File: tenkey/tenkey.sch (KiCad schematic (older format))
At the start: 53 parts, among them J1 USB, P1 SCK, P2 MISO, P3 MOSI, P4 RESET, P5 5V, P6 GND, SW0:0 NUM_0, SW0:2 DOT, SW1 RESET, SW1:0 NUM_1, SW1:1 NUM_2, SW1:2 NUM_3, SW1:3 ENTER, SW2:0 NUM_4, SW2:1 NUM_5, SW2:2 NUM_6, SW3:0 NUM_7, SW3:1 NUM_8, SW3:2 NUM_9, SW3:3 PLUS, SW4:0 NUM_LCK, SW4:1 DIVIDE, SW4:2 MULTIPLY, SW4:3 MINUS, U1 ATmega32U4-AU, X1 CRYSTAL

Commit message: changed some footprints to SMD
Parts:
- J1: symbol USB -> USB-Mini
- R3, R4: value R -> 22
- X1: value CRYSTAL -> 16 MHz
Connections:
- wire segments 58 -> 59
- no-connect marks 0 -> 1
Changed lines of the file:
@@
 	7750 2550 7750 2200
 $Comp
-L USB J1
+L USB-Mini J1
 U 1 1 57151B01
-P 900 3100
-F 0 "J1" H 1000 2800 60  0000 C CNN
-F 1 "USB" H 750 3300 60  0000 L CNN
-F 2 "" H 900 3100 60  0000 C CNN
-F 3 "" H 900 3100 60  0000 C CNN
-	1    900  3100
-	1    0    0    -1
-$EndComp
-Wire Wire Line
-	1350 3000 2300 3000
+P 800 3100
+F 0 "J1" H 800 2700 60  0000 C CNN
+F 1 "USB" H 650 3300 60  0000 L CNN
+F 2 "" H 800 3100 60  0000 C CNN
+F 3 "" H 800 3100 60  0000 C CNN
+	1    800  3100
+	1    0    0    -1
+$EndComp
+Wire Wire Line
+	1250 3000 2300 3000
 Wire Wire Line
 	1350 3000 1350 2400
@@
 P 1600 3100
 F 0 "R3" V 1680 3100 40  0000 C CNN
-F 1 "R" V 1607 3101 40  0000 C CNN
+F 1 "22" V 1607 3101 40  0000 C CNN
 F 2 "" V 1530 3100 30  0000 C CNN
 F 3 "" H 1600 3100 30  0000 C CNN
@@
 P 2050 3200
 F 0 "R4" V 2130 3200 40  0000 C CNN
-F 1 "R" V 2057 3201 40  0000 C CNN
+F 1 "22" V 2057 3201 40  0000 C CNN
 F 2 "" V 1980 3200 30  0000 C CNN
 F 3 "" H 2050 3200 30  0000 C CNN
@@
 $EndComp
 Wire Wire Line
-	1800 3200 1350 3200
+	1250 3200 1800 3200
 Wire Wire Line
 	1850 3100 2300 3100
@@
 L GND #PWR03
 U 1 1 57152027
-P 1350 3500
-F 0 "#PWR03" H 1350 3500 30  0001 C CNN
-F 1 "GND" H 1350 3430 30  0001 C CNN
-F 2 "" H 1350 3500 60  0000 C CNN
-F 3 "" H 1350 3500 60  0000 C CNN
-	1    1350 3500
+P 1250 3450
+F 0 "#PWR03" H 1250 3450 30  0001 C CNN
+F 1 "GND" H 1250 3380 30  0001 C CNN
+F 2 "" H 1250 3450 60  0000 C CNN
+F 3 "" H 1250 3450 60  0000 C CNN
+	1    1250 3450
 	1    0    0    -1
 $EndComp
@@
 P 1750 4700
 F 0 "X1" H 1750 4850 60  0000 C CNN
-F 1 "CRYSTAL" H 1750 4550 60  0000 C CNN
+F 1 "16 MHz" H 1750 4550 60  0000 C CNN
 F 2 "" H 1750 4700 60  0000 C CNN
 F 3 "" H 1750 4700 60  0000 C CNN
@@
 Wire Wire Line
 	1450 3300 1350 3300
-Wire Wire Line
-	1350 3300 1350 3450
 Connection ~ 1350 3300
 Wire Wire Line
 	1850 3300 2300 3300
 Wire Wire Line
-	1350 3400 2300 3400
-Connection ~ 1350 3400
+	1250 3400 2300 3400
+Connection ~ 1250 3400
 Connection ~ 1350 2400
 Connection ~ 1350 3000
@@
 Text Label 4750 2400 0    60   ~ 0
 SCK
-Text Label 1350 2400 0    60   ~ 0
-+5V
 $Comp
 L R R5
@@
 	1    0    0    -1
 $EndComp
+Wire Wire Line
+	1350 3300 1350 3400
+Connection ~ 1350 3400
+Wire Wire Line
+	1350 3100 1250 3100
+NoConn ~ 1250 3300
+Text Label 1600 2400 0    60   ~ 0
++5V
 $EndSCHEMATC

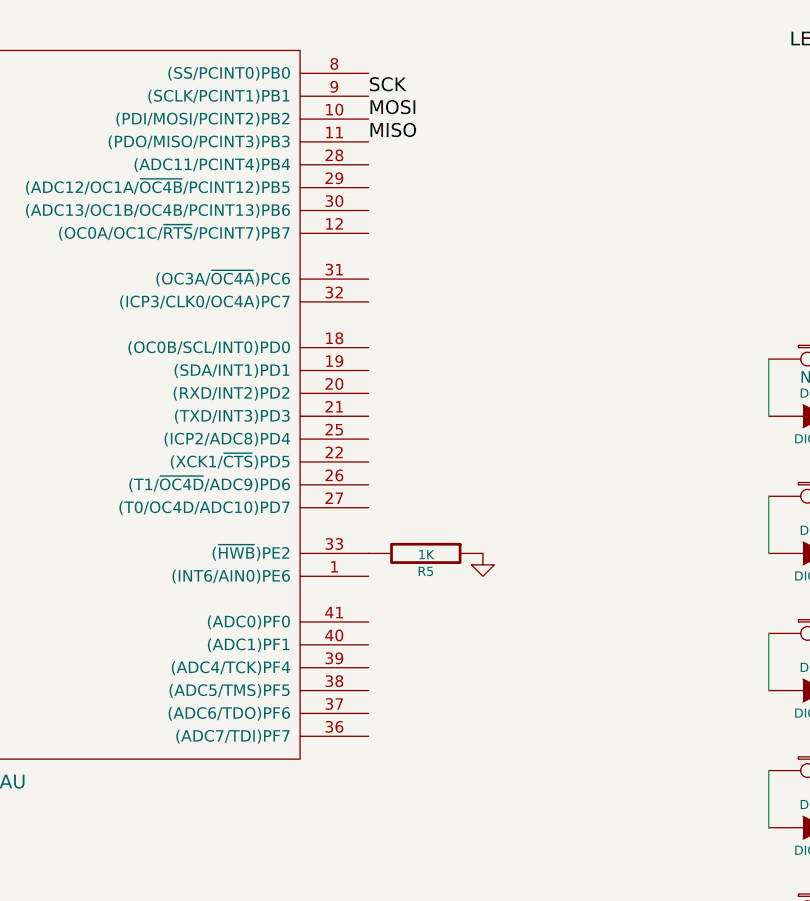
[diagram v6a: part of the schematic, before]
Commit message: PCB routing done, needs to check and reconcile footprints before ordering components
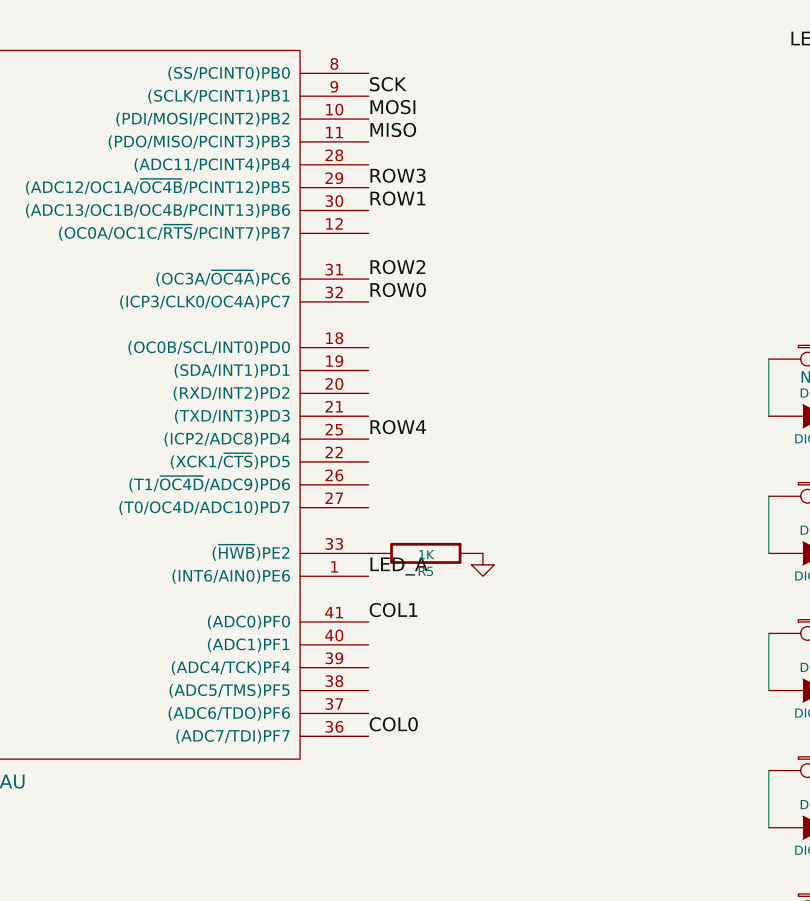
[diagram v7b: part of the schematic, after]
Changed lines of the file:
@@
 Text Label 1600 2400 0    60   ~ 0
 +5V
+Text Label 4750 4500 0    60   ~ 0
+LED_A
+Text Label 4750 4700 0    60   ~ 0
+COL1
+Text Label 4750 5200 0    60   ~ 0
+COL0
+Text Label 4750 3300 0    60   ~ 0
+ROW0
+Text Label 4750 3900 0    60   ~ 0
+ROW4
+Text Label 4750 3200 0    60   ~ 0
+ROW2
+Text Label 4750 2900 0    60   ~ 0
+ROW1
+Text Label 4750 2800 0    60   ~ 0
+ROW3
 $EndSCHEMATC

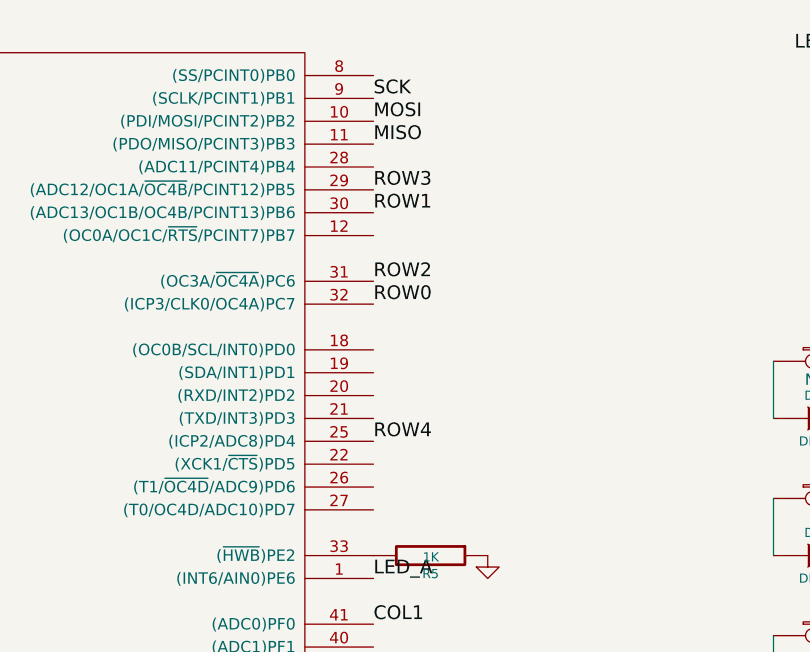
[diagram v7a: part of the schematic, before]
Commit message: connected ROW2 and ROW3 to ATMEGA32U4 and added mounting holes
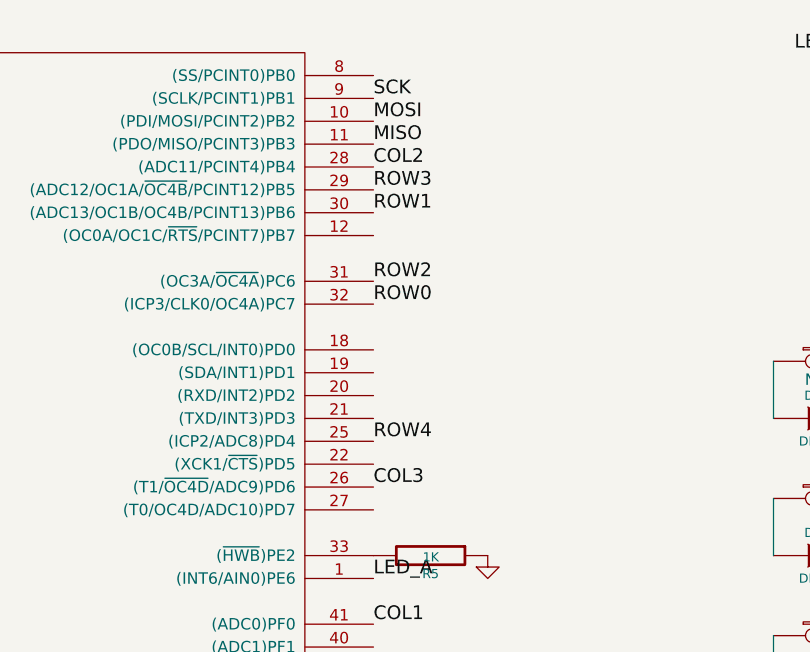
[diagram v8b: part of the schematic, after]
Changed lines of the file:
@@
 Text Label 4750 2800 0    60   ~ 0
 ROW3
+Text Label 4750 2700 0    60   ~ 0
+COL2
+Text Label 4750 4100 0    60   ~ 0
+COL3
 $EndSCHEMATC
